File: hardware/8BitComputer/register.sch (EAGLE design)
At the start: 51 parts, among them IC1 SN74LS173ANG4, IC2 SN74LS173ANG4, IC3 SN74LS245NE4, IC4 SN74LS173ANG4, IC5 SN74LS173ANG4, IC6 SN74LS245NE4, J1 BUS OUT, J2 pwr, J4 BUS OUT

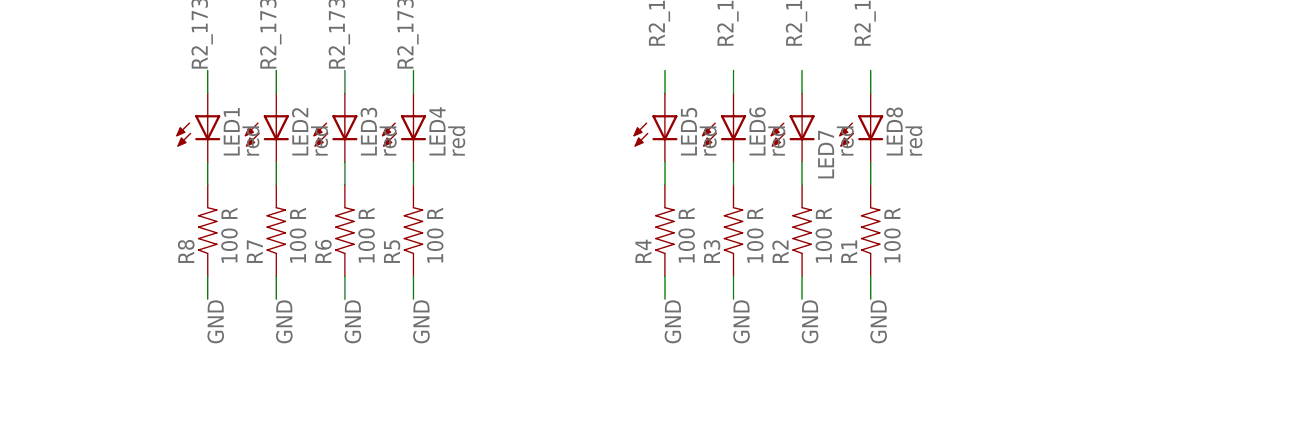
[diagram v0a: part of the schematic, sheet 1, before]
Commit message: adding static ram chip updated all other boards to remove led resistors that aren't needed
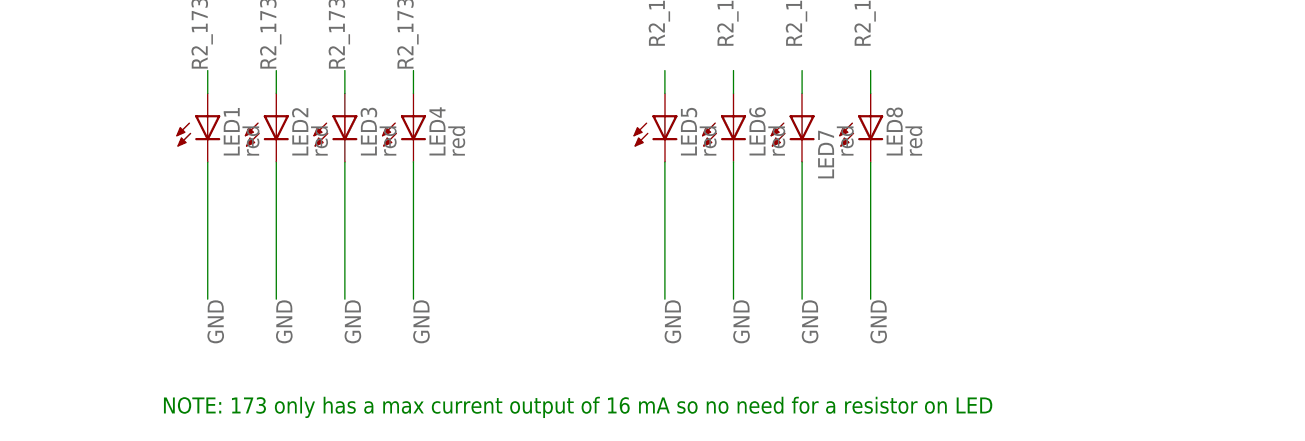
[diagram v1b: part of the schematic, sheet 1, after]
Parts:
- removed R1, R10, R11, R12, R13, R14, R15, R16, R2, R3, R4, R5, R6, R7, R8, R9: 100 R, passives:RESISTOR0805-RES
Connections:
- removed net N$1: LED9.C, R16.2
- removed net N$2: LED10.C, R15.2
- removed net N$27: LED1.C, R8.2
- removed net N$28: LED2.C, R7.2
- removed net N$29: LED3.C, R6.2
- removed net N$3: LED11.C, R14.2
- removed net N$30: LED4.C, R5.2
- removed net N$31: LED5.C, R4.2
- removed net N$32: LED6.C, R3.2
- removed net N$33: LED7.C, R2.2
- removed net N$34: LED8.C, R1.2
- removed net N$4: LED12.C, R13.2
- removed net N$5: LED13.C, R12.2
- removed net N$6: LED14.C, R11.2
- removed net N$7: LED15.C, R10.2
- removed net N$8: LED16.C, R9.2
- net GND: now also LED1.C, LED10.C, LED11.C, LED12.C, LED13.C, LED14.C, LED15.C, LED16.C, LED2.C, LED3.C, LED4.C, LED5.C, LED6.C, LED7.C, LED8.C, LED9.C; no longer R1.1, R10.1, R11.1, R12.1, R13.1, R14.1, R15.1, R16.1, R2.1, R3.1, R4.1, R5.1, R6.1, R7.1, R8.1, R9.1
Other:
- note added: "NOTE: 173 only has a max current output of 16 mA so no need for a resistor on LED"
